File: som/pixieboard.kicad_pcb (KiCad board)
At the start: 8 copper layers, 50 x 50 mm, 54 parts, among them J1 Conn_02x20_Counter_Clockwise, J2 Conn_02x20_Counter_Clockwise, J3 Conn_02x20_Counter_Clockwise, J4 Conn_02x20_Counter_Clockwise, SW1 SW_DIP_x03, U1 XC7A200T-3FBG484E, U2 AS4C256M16D3, U3 AS4C256M16D3

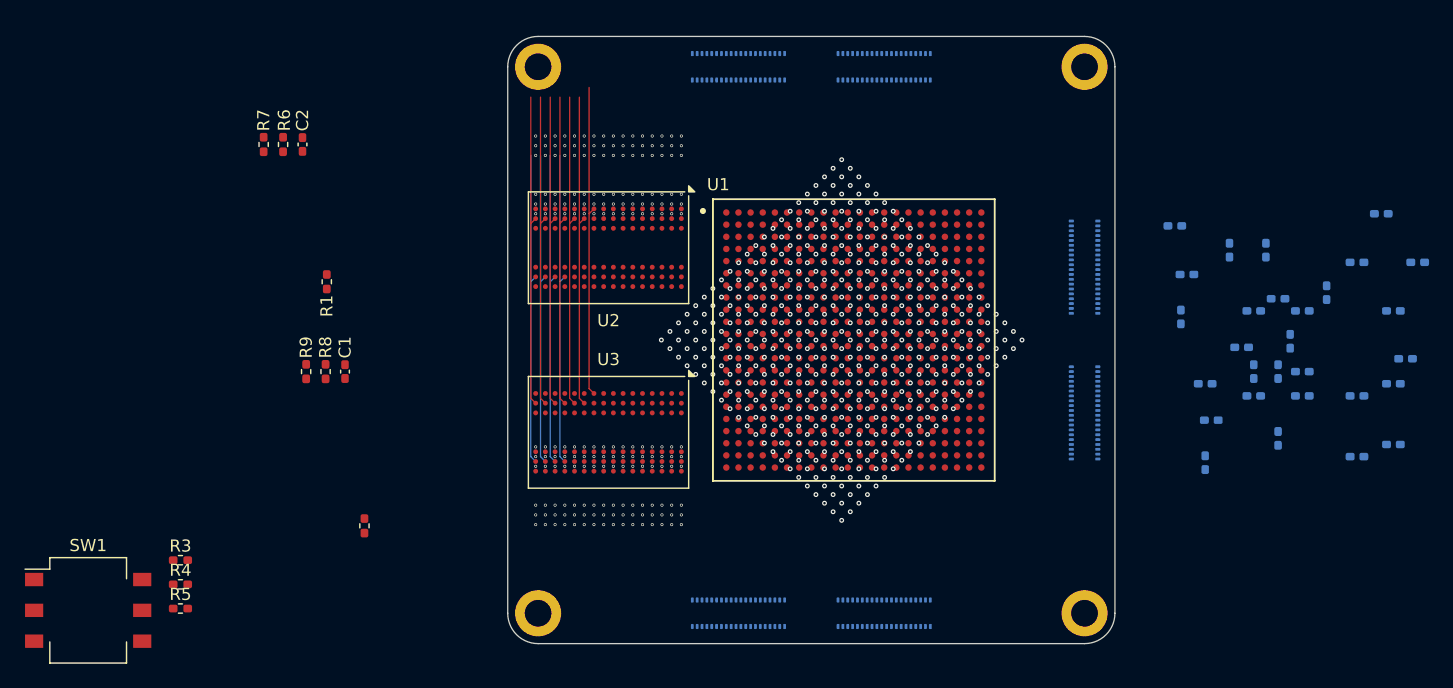
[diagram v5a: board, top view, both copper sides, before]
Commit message: Le DDR3 control traces
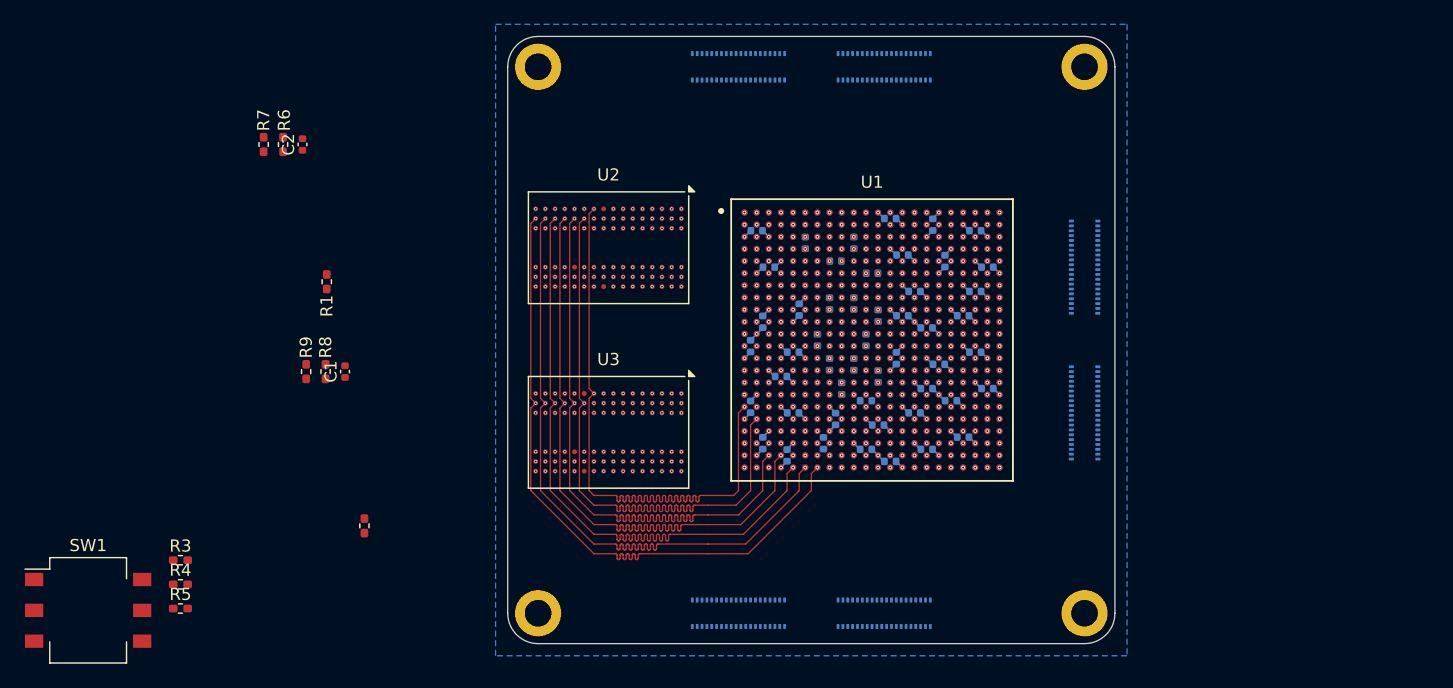
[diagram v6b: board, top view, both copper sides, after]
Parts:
- added C32: 100nF, Capacitor_SMD:C_0402_1005Metric, B.Cu at (-0.50, -6.50)
- added C33: 100nF, Capacitor_SMD:C_0402_1005Metric, B.Cu at (-0.50, 6.50)
- added C34: 100nF, Capacitor_SMD:C_0402_1005Metric, B.Cu at (9.00, 5.00)
- added C35: 100nF, Capacitor_SMD:C_0402_1005Metric, B.Cu at (12.0, 4.00)
- added C36: 100nF, Capacitor_SMD:C_0402_1005Metric, B.Cu at (7.00, -1.00)
- added C37: 100nF, Capacitor_SMD:C_0402_1005Metric, B.Cu at (6.00, -4.00)
- added C38: 100nF, Capacitor_SMD:C_0402_1005Metric, B.Cu at (11.0, -9.00)
- added C39: 100nF, Capacitor_SMD:C_0402_1005Metric, B.Cu at (5.00, -7.00)
- added C40: 100nF, Capacitor_SMD:C_0402_1005Metric, B.Cu at (4.50, 1.50)
- added C41: 100nF, Capacitor_SMD:C_0402_1005Metric, B.Cu at (11.0, 1.00)
- added C42: 100nF, Capacitor_SMD:C_0402_1005Metric, B.Cu at (12.0, -6.00)
- added C43: 100nF, Capacitor_SMD:C_0402_1005Metric, B.Cu at (3.00, 7.00)
- added C44: 100nF, Capacitor_SMD:C_0402_1005Metric, B.Cu at (6.00, 6.00)
- added C45: 100nF, Capacitor_SMD:C_0402_1005Metric, B.Cu at (4.00, 10.0)
- added C46: 100nF, Capacitor_SMD:C_0402_1005Metric, B.Cu at (2.00, 5.00)
- added C47: 100nF, Capacitor_SMD:C_0402_1005Metric, B.Cu at (-3.50, -2.50)
- added C48: 100nF, Capacitor_SMD:C_0402_1005Metric, B.Cu at (-4.00, 1.00)
- added C49: 100nF, Capacitor_SMD:C_0402_1005Metric, B.Cu at (-7.50, 0.50)
- added C50: 100nF, Capacitor_SMD:C_0402_1005Metric, B.Cu at (-7.50, 5.50)
- added C51: 100nF, Capacitor_SMD:C_0402_1005Metric, B.Cu at (-1.50, 8.50)
- added C52: 100nF, Capacitor_SMD:C_0402_1005Metric, B.Cu at (-6.50, 8.50)
- C1, C10, C11, C12, C13, C14, C15, C16, C17, C18, C19, C2, C20, C21, C22, C23, C24, C25, C26, C27, C28, C29, C3, C30, C31, C4, C5, C6, C7, C8, C9: footprint Capacitor_SMD:C_0402_1005Metric_Pad0.74x0.62mm_HandSolder -> Capacitor_SMD:C_0402_1005Metric
- moved C18 40.4 mm to (4.00, -10.0), turned to 180 degrees
- moved C21 40.4 mm to (5.00, -2.00), turned to 0 degrees
- moved C20 38.9 mm to (8.50, -6.50), turned to -90 degrees
- moved C25 37.5 mm to (8.00, 2.00), turned to 180 degrees
- moved C27 36.8 mm to (2.50, -5.50)
- moved C23 36.6 mm to (10.0, -2.00)
- moved C24 35.4 mm to (10.0, 8.00)
- moved C26 35.4 mm to (7.00, 4.00)
- moved C28 35.4 mm to (7.00, 9.00)
- moved C19 35.1 mm to (7.50, -9.50), turned to -90 degrees
- moved C16 34.9 mm to (-5.00, 3.00)
- moved C9 34.9 mm to (-3.00, -8.00), turned to 90 degrees
- moved C4 34.9 mm to (-1.00, -3.00), turned to -90 degrees
- moved C5 34.9 mm to (-2.00, 0.00), turned to -90 degrees
- moved C7 34.9 mm to (1.00, 2.00), turned to 90 degrees
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- renumbered J3 to J5, J4 to J6
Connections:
- J5 pad 1: unconnected-(J3-Pin_1-Pad1) -> unconnected-(J5-Pin_1-Pad1)
- J5 pad 10: unconnected-(J3-Pin_10-Pad10) -> unconnected-(J5-Pin_10-Pad10)
- J5 pad 11: unconnected-(J3-Pin_11-Pad11) -> unconnected-(J5-Pin_11-Pad11)
- J5 pad 12: unconnected-(J3-Pin_12-Pad12) -> unconnected-(J5-Pin_12-Pad12)
- J5 pad 13: unconnected-(J3-Pin_13-Pad13) -> unconnected-(J5-Pin_13-Pad13)
- J5 pad 14: unconnected-(J3-Pin_14-Pad14) -> unconnected-(J5-Pin_14-Pad14)
- J5 pad 15: unconnected-(J3-Pin_15-Pad15) -> unconnected-(J5-Pin_15-Pad15)
- J5 pad 16: unconnected-(J3-Pin_16-Pad16) -> unconnected-(J5-Pin_16-Pad16)
- J5 pad 17: unconnected-(J3-Pin_17-Pad17) -> unconnected-(J5-Pin_17-Pad17)
- J5 pad 18: unconnected-(J3-Pin_18-Pad18) -> unconnected-(J5-Pin_18-Pad18)
- J5 pad 19: unconnected-(J3-Pin_19-Pad19) -> unconnected-(J5-Pin_19-Pad19)
- J5 pad 2: unconnected-(J3-Pin_2-Pad2) -> unconnected-(J5-Pin_2-Pad2)
- J5 pad 20: unconnected-(J3-Pin_20-Pad20) -> unconnected-(J5-Pin_20-Pad20)
- J5 pad 21: unconnected-(J3-Pin_21-Pad21) -> unconnected-(J5-Pin_21-Pad21)
- J5 pad 22: unconnected-(J3-Pin_22-Pad22) -> unconnected-(J5-Pin_22-Pad22)
- J5 pad 23: unconnected-(J3-Pin_23-Pad23) -> unconnected-(J5-Pin_23-Pad23)
- J5 pad 24: unconnected-(J3-Pin_24-Pad24) -> unconnected-(J5-Pin_24-Pad24)
- J5 pad 25: unconnected-(J3-Pin_25-Pad25) -> unconnected-(J5-Pin_25-Pad25)
- J5 pad 26: unconnected-(J3-Pin_26-Pad26) -> unconnected-(J5-Pin_26-Pad26)
- J5 pad 27: unconnected-(J3-Pin_27-Pad27) -> unconnected-(J5-Pin_27-Pad27)
- J5 pad 28: unconnected-(J3-Pin_28-Pad28) -> unconnected-(J5-Pin_28-Pad28)
- J5 pad 29: unconnected-(J3-Pin_29-Pad29) -> unconnected-(J5-Pin_29-Pad29)
- J5 pad 3: unconnected-(J3-Pin_3-Pad3) -> unconnected-(J5-Pin_3-Pad3)
- J5 pad 30: unconnected-(J3-Pin_30-Pad30) -> unconnected-(J5-Pin_30-Pad30)
- J5 pad 31: unconnected-(J3-Pin_31-Pad31) -> unconnected-(J5-Pin_31-Pad31)
- J5 pad 32: unconnected-(J3-Pin_32-Pad32) -> unconnected-(J5-Pin_32-Pad32)
- J5 pad 33: unconnected-(J3-Pin_33-Pad33) -> unconnected-(J5-Pin_33-Pad33)
- J5 pad 34: unconnected-(J3-Pin_34-Pad34) -> unconnected-(J5-Pin_34-Pad34)
- J5 pad 35: unconnected-(J3-Pin_35-Pad35) -> unconnected-(J5-Pin_35-Pad35)
- J5 pad 36: unconnected-(J3-Pin_36-Pad36) -> unconnected-(J5-Pin_36-Pad36)
- J5 pad 37: unconnected-(J3-Pin_37-Pad37) -> unconnected-(J5-Pin_37-Pad37)
- J5 pad 38: unconnected-(J3-Pin_38-Pad38) -> unconnected-(J5-Pin_38-Pad38)
- J5 pad 39: unconnected-(J3-Pin_39-Pad39) -> unconnected-(J5-Pin_39-Pad39)
- J5 pad 4: unconnected-(J3-Pin_4-Pad4) -> unconnected-(J5-Pin_4-Pad4)
- J5 pad 40: unconnected-(J3-Pin_40-Pad40) -> unconnected-(J5-Pin_40-Pad40)
- J5 pad 5: unconnected-(J3-Pin_5-Pad5) -> unconnected-(J5-Pin_5-Pad5)
- J5 pad 6: unconnected-(J3-Pin_6-Pad6) -> unconnected-(J5-Pin_6-Pad6)
- J5 pad 7: unconnected-(J3-Pin_7-Pad7) -> unconnected-(J5-Pin_7-Pad7)
- J5 pad 8: unconnected-(J3-Pin_8-Pad8) -> unconnected-(J5-Pin_8-Pad8)
- J5 pad 9: unconnected-(J3-Pin_9-Pad9) -> unconnected-(J5-Pin_9-Pad9)
- J6 pad 1: unconnected-(J4-Pin_1-Pad1) -> unconnected-(J6-Pin_1-Pad1)
- J6 pad 10: unconnected-(J4-Pin_10-Pad10) -> unconnected-(J6-Pin_10-Pad10)
- J6 pad 11: unconnected-(J4-Pin_11-Pad11) -> unconnected-(J6-Pin_11-Pad11)
- J6 pad 12: unconnected-(J4-Pin_12-Pad12) -> unconnected-(J6-Pin_12-Pad12)
- J6 pad 13: unconnected-(J4-Pin_13-Pad13) -> unconnected-(J6-Pin_13-Pad13)
- J6 pad 14: unconnected-(J4-Pin_14-Pad14) -> unconnected-(J6-Pin_14-Pad14)
- J6 pad 15: unconnected-(J4-Pin_15-Pad15) -> unconnected-(J6-Pin_15-Pad15)
- J6 pad 16: unconnected-(J4-Pin_16-Pad16) -> unconnected-(J6-Pin_16-Pad16)
- J6 pad 17: unconnected-(J4-Pin_17-Pad17) -> unconnected-(J6-Pin_17-Pad17)
- J6 pad 18: unconnected-(J4-Pin_18-Pad18) -> unconnected-(J6-Pin_18-Pad18)
- J6 pad 19: unconnected-(J4-Pin_19-Pad19) -> unconnected-(J6-Pin_19-Pad19)
- J6 pad 2: unconnected-(J4-Pin_2-Pad2) -> unconnected-(J6-Pin_2-Pad2)
- J6 pad 20: unconnected-(J4-Pin_20-Pad20) -> unconnected-(J6-Pin_20-Pad20)
- J6 pad 21: unconnected-(J4-Pin_21-Pad21) -> unconnected-(J6-Pin_21-Pad21)
- J6 pad 22: unconnected-(J4-Pin_22-Pad22) -> unconnected-(J6-Pin_22-Pad22)
- J6 pad 23: unconnected-(J4-Pin_23-Pad23) -> unconnected-(J6-Pin_23-Pad23)
- J6 pad 24: unconnected-(J4-Pin_24-Pad24) -> unconnected-(J6-Pin_24-Pad24)
- J6 pad 25: unconnected-(J4-Pin_25-Pad25) -> unconnected-(J6-Pin_25-Pad25)
- J6 pad 26: unconnected-(J4-Pin_26-Pad26) -> unconnected-(J6-Pin_26-Pad26)
- J6 pad 27: unconnected-(J4-Pin_27-Pad27) -> unconnected-(J6-Pin_27-Pad27)
- J6 pad 28: unconnected-(J4-Pin_28-Pad28) -> unconnected-(J6-Pin_28-Pad28)
- J6 pad 29: unconnected-(J4-Pin_29-Pad29) -> unconnected-(J6-Pin_29-Pad29)
- J6 pad 3: unconnected-(J4-Pin_3-Pad3) -> unconnected-(J6-Pin_3-Pad3)
- J6 pad 30: unconnected-(J4-Pin_30-Pad30) -> unconnected-(J6-Pin_30-Pad30)
- J6 pad 31: unconnected-(J4-Pin_31-Pad31) -> unconnected-(J6-Pin_31-Pad31)
- J6 pad 32: unconnected-(J4-Pin_32-Pad32) -> unconnected-(J6-Pin_32-Pad32)
- J6 pad 33: unconnected-(J4-Pin_33-Pad33) -> unconnected-(J6-Pin_33-Pad33)
- J6 pad 34: unconnected-(J4-Pin_34-Pad34) -> unconnected-(J6-Pin_34-Pad34)
- J6 pad 35: unconnected-(J4-Pin_35-Pad35) -> unconnected-(J6-Pin_35-Pad35)
- J6 pad 36: unconnected-(J4-Pin_36-Pad36) -> unconnected-(J6-Pin_36-Pad36)
- J6 pad 37: unconnected-(J4-Pin_37-Pad37) -> unconnected-(J6-Pin_37-Pad37)
- J6 pad 38: unconnected-(J4-Pin_38-Pad38) -> unconnected-(J6-Pin_38-Pad38)
- J6 pad 39: unconnected-(J4-Pin_39-Pad39) -> unconnected-(J6-Pin_39-Pad39)
- J6 pad 4: unconnected-(J4-Pin_4-Pad4) -> unconnected-(J6-Pin_4-Pad4)
- J6 pad 40: unconnected-(J4-Pin_40-Pad40) -> unconnected-(J6-Pin_40-Pad40)
- J6 pad 5: unconnected-(J4-Pin_5-Pad5) -> unconnected-(J6-Pin_5-Pad5)
- J6 pad 6: unconnected-(J4-Pin_6-Pad6) -> unconnected-(J6-Pin_6-Pad6)
- J6 pad 7: unconnected-(J4-Pin_7-Pad7) -> unconnected-(J6-Pin_7-Pad7)
- J6 pad 8: unconnected-(J4-Pin_8-Pad8) -> unconnected-(J6-Pin_8-Pad8)
- J6 pad 9: unconnected-(J4-Pin_9-Pad9) -> unconnected-(J6-Pin_9-Pad9)
- U1 pad AA3: /DDR3/DDR_BA2 -> /DDR3/DDR_BA0
- U1 pad AA4: /DDR3/DDR_A5 -> /DDR3/DDR_A3
- U1 pad AA6: /DDR3/DDR_A7 -> /DDR3/DDR_A2
- U1 pad AB3: /DDR3/DDR_A3 -> unconnected-(U1E-IO_L8P_T1_34-PadAB3)
- U1 pad AB5: /DDR3/DDR_A2 -> /DDR3/DDR_A5
- U1 pad AB6: /DDR3/~{DDR_RST} -> /DDR3/DDR_A7
- U1 pad AB7: /DDR3/DDR_A9 -> /DDR3/~{DDR_RST}
- U1 pad R6: /DDR3/DDR_A12 -> /DDR3/DDR_CLK_E
- U1 pad T1: /DDR3/DDR_CLK_E -> /DDR3/~{DDR_RAS}
- U1 pad T4: /DDR3/DDR_A10 -> /DDR3/DDR_A4
- U1 pad T6: /DDR3/DDR_A1 -> /DDR3/DDR_A10
- U1 pad U2: /DDR3/DDR_BA1 -> /DDR3/~{DDR_CAS}
- U1 pad U3: /DDR3/DDR_A4 -> unconnected-(U1E-IO_L6P_T0_34-PadU3)
- U1 pad V4: unconnected-(U1E-IO_L12P_T1_MRCC_34-PadV4) -> /DDR3/DDR_A12
- U1 pad V5: unconnected-(U1E-IO_L16N_T2_34-PadV5) -> /DDR3/DDR_A1
- U1 pad V7: /DDR3/DDR_A11 -> unconnected-(U1E-IO_L19P_T3_34-PadV7)
- U1 pad W1: /DDR3/~{DDR_RAS} -> unconnected-(U1E-IO_L5P_T0_34-PadW1)
- U1 pad W2: /DDR3/DDR_BA0 -> /DDR3/DDR_BA1
- U1 pad W6: unconnected-(U1E-IO_L15P_T2_DQS_34-PadW6) -> /DDR3/DDR_A11
- U1 pad W7: unconnected-(U1E-IO_L19N_T3_VREF_34-PadW7) -> /DDR3/DDR_A14
- U1 pad Y2: /DDR3/~{DDR_CAS} -> unconnected-(U1E-IO_L4N_T0_34-PadY2)
- U1 pad Y4: unconnected-(U1E-IO_L11P_T1_SRCC_34-PadY4) -> /DDR3/DDR_BA2
- U1 pad Y7: unconnected-(U1E-IO_L23N_T3_34-PadY7) -> /DDR3/DDR_A9
- U1 pad Y8: /DDR3/DDR_A14 -> unconnected-(U1E-IO_L23P_T3_34-PadY8)
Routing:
- net /DDR3/~{DDR_RST}: track 25.9 -> 55.5 mm, vias 4 -> 3
- net /DDR3/DDR_A7: track 25.9 -> 55.4 mm
- net /DDR3/DDR_A5: track 25.9 -> 55.4 mm
- net /DDR3/DDR_A3: track 25.9 -> 55.4 mm
- net /DDR3/DDR_BA0: track 25.9 -> 55.3 mm
- net /DDR3/~{DDR_CS}: track 25.9 -> 55.3 mm, vias 4 -> 3
- net /DDR3/DDR_ODT: track 25.9 -> 55.3 mm, vias 6 -> 3
- net /DDR3/DDR_A13: track 25.9 -> 55.0 mm, vias 2 -> 3
- net /DDR3/DDR_A9: track 25.9 -> 55.0 mm, vias 0 -> 3
- net /DDR3/DDR_A2: track 25.9 -> 54.9 mm, vias 1 -> 3
- net /DDR3/DDR_A0: track 25.9 -> 54.9 mm, vias 2 -> 3
- net /DDR3/DDR_BA2: track 25.9 -> 54.9 mm, vias 1 -> 3
- net /DDR3/~{DDR_CAS}: track 25.9 -> 54.9 mm, vias 1 -> 3
- net /DDR3/~{DDR_WE}: track 25.9 -> 54.8 mm, vias 1 -> 3
- net /DDR3/~{DDR_RAS}: track 25.9 -> 54.8 mm, vias 1 -> 3
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- added copper zone on B.Cu, net GND
- added copper zone on In5.Cu, net GND
- removed copper zone on In4.Cu, net GND
- removed copper zone on In6.Cu, net GND
